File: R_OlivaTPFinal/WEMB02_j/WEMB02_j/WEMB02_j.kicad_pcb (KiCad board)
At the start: 2 copper layers, 164 x 139 mm, 97 parts, among them J201 Conn_01x05, J202 RasPI_IO_Header, J203 RS485, J301 EXP_PWR, Q201 IRFR9024, Q301 BC817-40_215, Q302 BC817-40_215, Q401 MMBTA42LT1G, U201 SN75HVD08, U301 SDM30-125S, U302 FEEDER_BRD, U303 R-78E3.3-0.5, U304 R-78E5.0-1.0, U401 ICL7665ACSA+

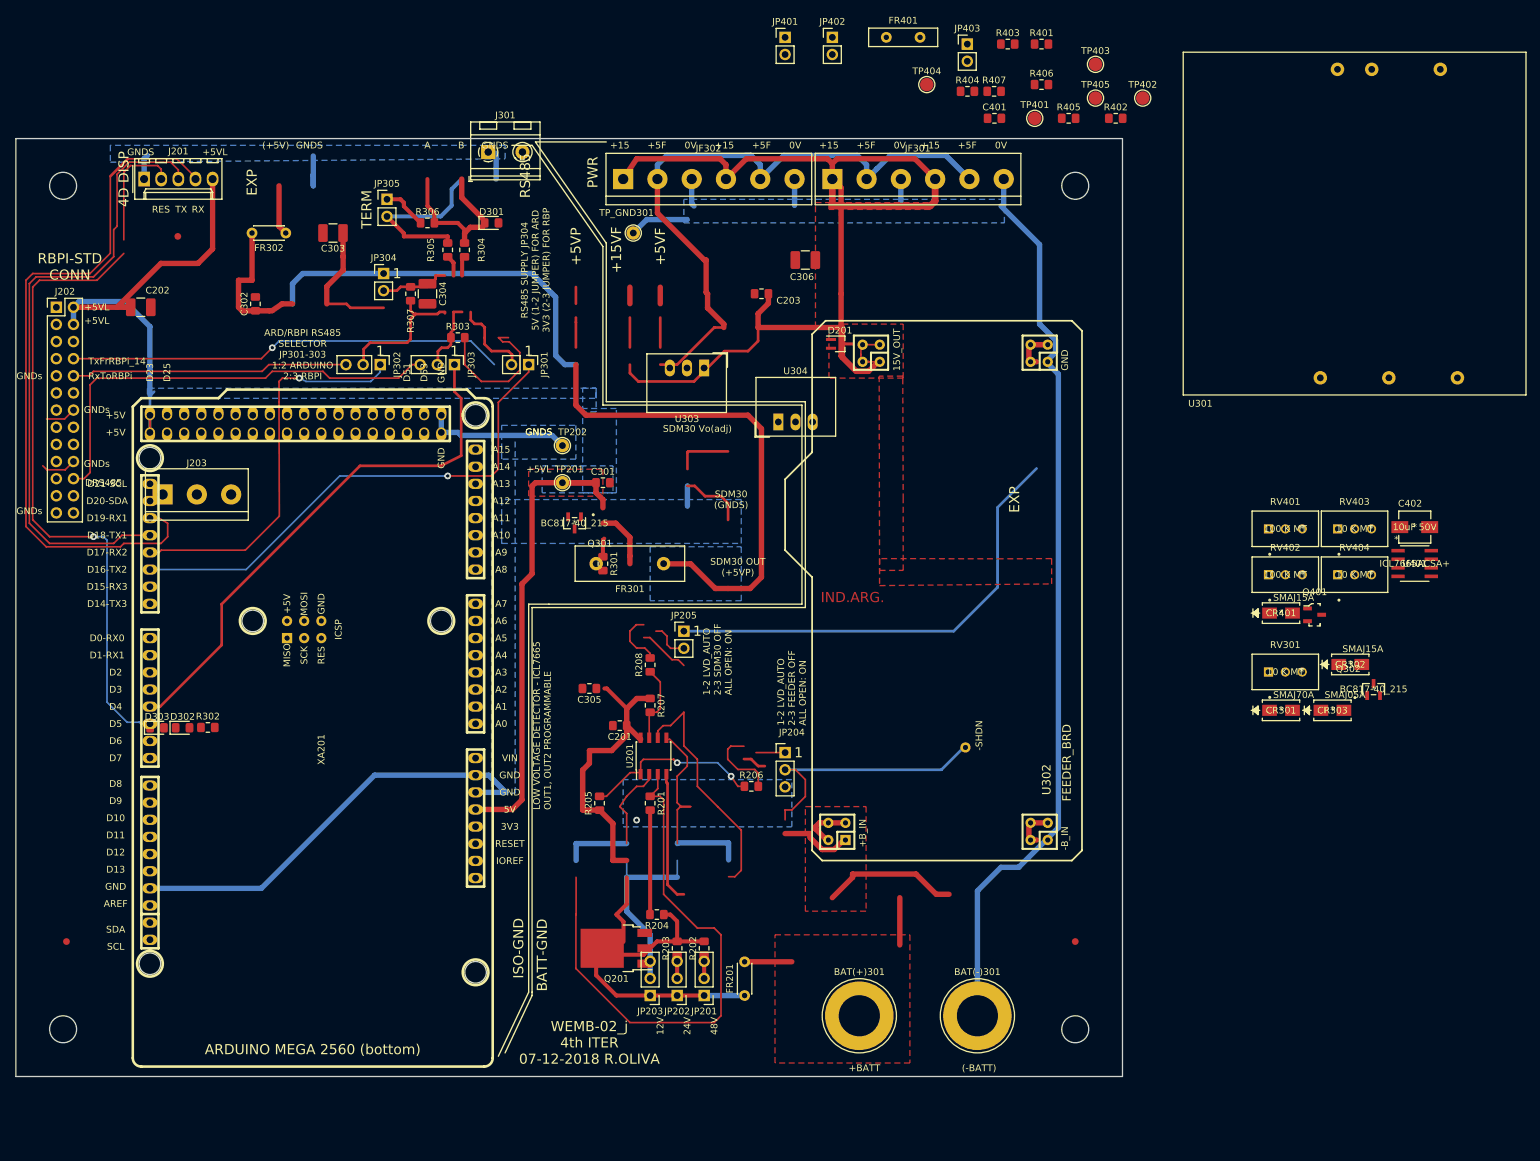
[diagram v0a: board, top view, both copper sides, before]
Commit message: WEMB02-J Sch + PCB completos, faltan algunos mod.3D
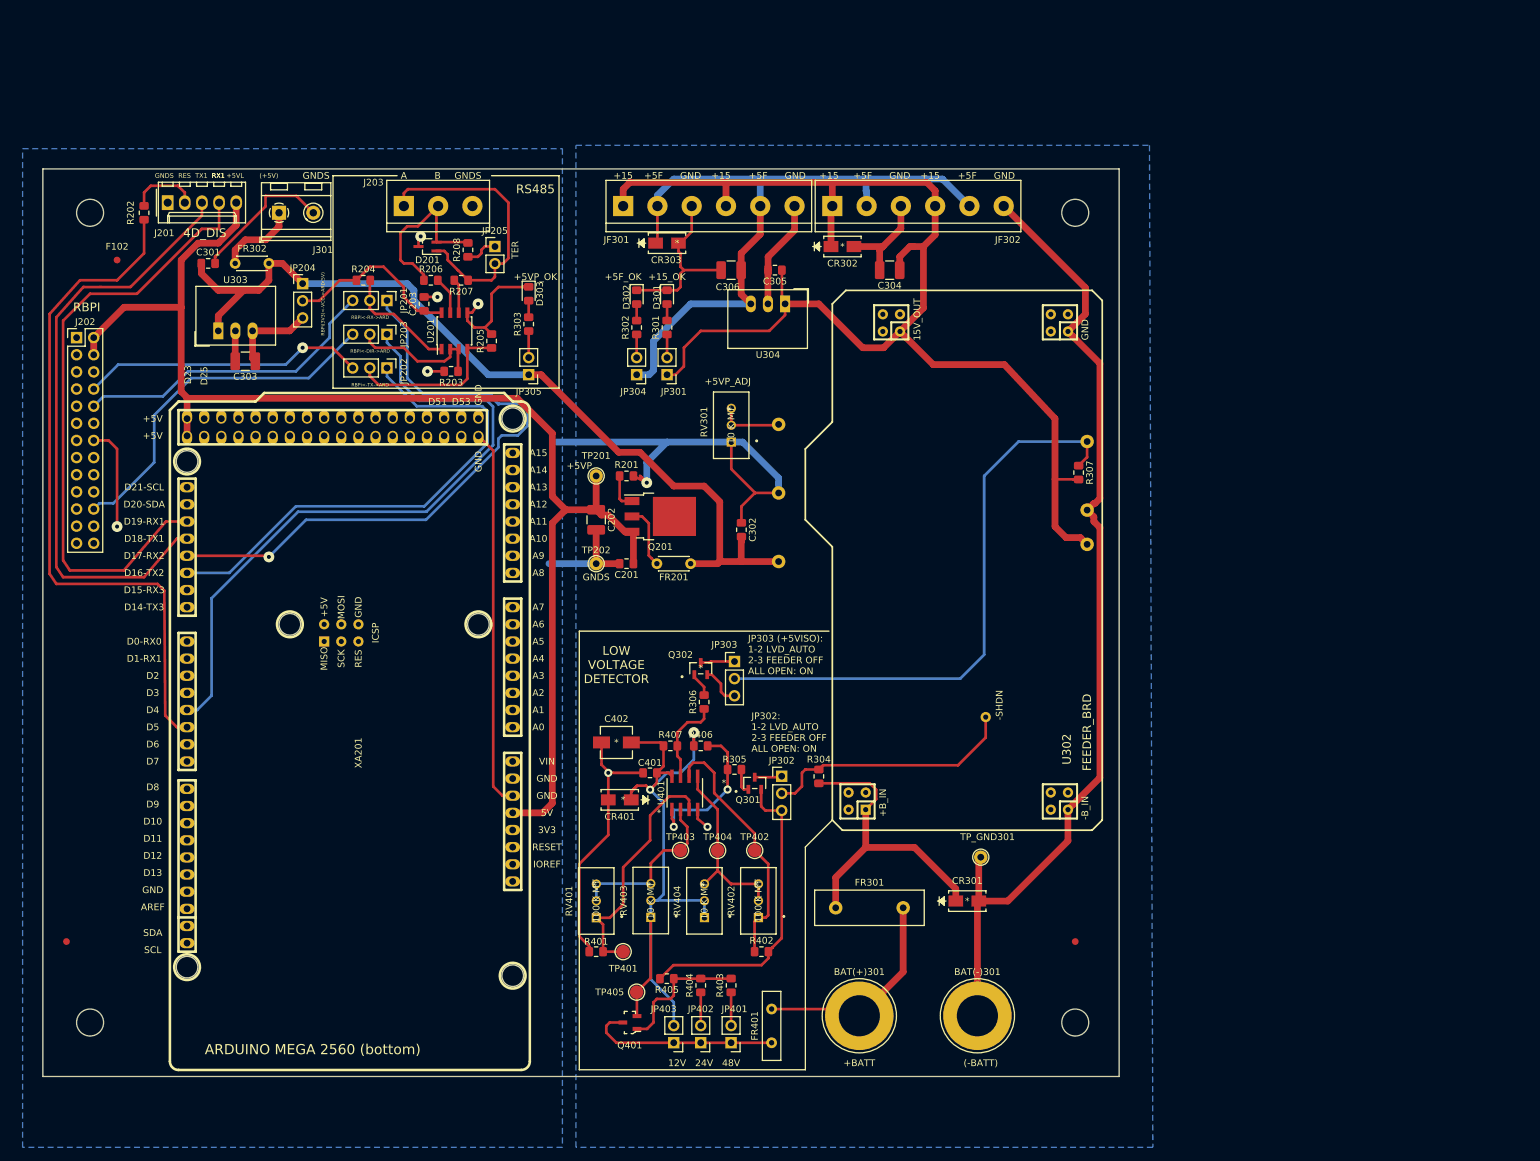
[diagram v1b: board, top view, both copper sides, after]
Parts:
- U301: moved to B.Cu
- moved JP403 154.3 mm to (158.5, 155.0), turned to 180 degrees
- moved JP402 150.3 mm to (162.5, 155.0), turned to 180 degrees
- moved FR401 150.0 mm to (173.0, 155.0), turned to 90 degrees
- moved R401 149.8 mm to (147.0, 141.5), turned to 180 degrees
- moved JP401 149.2 mm to (167.0, 155.0), turned to 180 degrees
- moved TP405 148.9 mm to (153.0, 147.5)
- moved R403 145.4 mm to (167.0, 146.5), turned to 90 degrees
- moved R405 140.7 mm to (157.5, 145.5), turned to 180 degrees
- moved R404 138.3 mm to (162.5, 146.5), turned to 90 degrees
- moved TP401 137.7 mm to (151.0, 141.5)
- moved R202 137.0 mm to (80.0, 32.0), turned to 270 degrees
- moved R402 134.2 mm to (171.5, 141.5)
- moved TP403 131.7 mm to (159.5, 126.5)
- moved TP402 125.5 mm to (170.5, 126.5)
- moved C402 122.5 mm to (150.0, 110.5), turned to 180 degrees
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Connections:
- JP403 pad 1: /LowV_Detect/+B_LVD -> Net-(FR401-Pad1)
- JP403 pad 2: Net-(FR401-Pad1) -> /LowV_Detect/+B_LVD
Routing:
- net +5VP: track 25.8 -> 132.8 mm
- net Earth: track 191.6 -> 297.5 mm, vias 1 -> 2
- net Net-(R202-Pad2): track 0.00 -> 102.0 mm
- net /LowV_Detect/+B_LVD: track 0.00 -> 99.3 mm, vias 0 -> 2
- net Net-(R213-Pad2): track 94.0 -> 0.00 mm, vias 1 -> 0
- net /Power/SDM_ON: track 0.00 -> 86.4 mm
- net /Power/V+_Q_EMIT: track 83.6 -> 0.00 mm
- net /Power/SET1_IN: track 81.9 -> 0.00 mm
- net Net-(JP205-Pad1): track 69.2 -> 4.92 mm
- net GNDS: track 143.5 -> 206.6 mm, vias 0 -> 6
- net /Power/+B_FEED: track 107.5 -> 46.6 mm
- net +5F: track 154.4 -> 104.3 mm
- net +5VL: track 150.3 -> 197.6 mm
- net /Power/-FSHDN: track 0.00 -> 37.9 mm
- net Net-(R402-Pad1): track 0.00 -> 37.3 mm
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- removed copper zone on F.Cu, net +15V
- removed copper zone on B.Cu, net +5VL
- removed copper zone on F.Cu, net +5VL
- removed copper zone on B.Cu, net +5VP
- removed copper zone on F.Cu, net /Power/+B_FEED
- removed copper zone on F.Cu, net /Power/BAT+
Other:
- board size 164 x 139 mm -> 159.5 x 134.5 mm
- rule trace_min: 0.2 -> 0.4
- rule via_min_drill: 0.3 -> 0.6
- rule via_min_size: 0.4 -> 1.2
- board text added: "+15_OK"
- board text added: "+5F_OK"
- board text added: "+5VP_ADJ"
- board text added: "+5VP_OK"
- board text added: "4D_DIS"
- board text added: "GND"
- board text added: "Grilla 1 mmPos / 0.5 mm ruteo. Pista 0.4mm. Margen: 0,4 mm. Vías: 1,2 / 0,6mm Fabricación en Mayer S.A. FR4 doble lado 1oz"
- board text added: "JP302: 1-2 LVD_AUTO 2-3 FEEDER OFF ALL OPEN: ON"
- board text added: "JP303 (+5VISO): 1-2 LVD_AUTO 2-3 FEEDER OFF ALL OPEN: ON"
- board text added: "LOW VOLTAGE DETECTOR"
- board text added: "RBPI"
- board text added: "RBPi(3V3)<-VCC->ARD(5V)"
- board text added: "RBPi<-DIR->ARD"
- board text added: "RBPi<-RX->ARD"
- board text added: "RBPi<-TX->ARD"
- board text added: "RX1"
- board text added: "TER"
- board text added: "TX1"
- board text removed: "+15VF"
- board text removed: "+5VF"
- board text removed: "0V"
- board text removed: "1"
- board text removed: "1-2 LVD_AUTO 2-3 FEEDER OFF ALL OPEN: ON"
- board text removed: "1-2 LVD_AUTO 2-3 SDM30 OFF ALL OPEN: ON"
- board text removed: "4D DISP"
- board text removed: "ARD/RBPI RS485 SELECTOR JP301-303 1:2 ARDUINO 2:3 RBPI"
- board text removed: "BATT-GND"
- board text removed: "DRS485"
- board text removed: "EXP"
- board text removed: "GNDs"
- board text removed: "Grilla 1 mmPos / 0.5 mm ruteo. Pista 0.25mm. Margen: 0,25 mm. Vías: 1 / 0,5mm Fabricación en Mayer S.A. FR4 doble lado 1oz"
- board text removed: "IND.ARG."
- board text removed: "ISO-GND"
- board text removed: "LOW VOLTAGE DETECTOR - ICL7665 OUT1, OUT2 PROGRAMMABLE"
- board text removed: "PWR"
- board text removed: "RBPI-STD CONN"
- board text removed: "RS485 SUPPLY JP304 5V (1-2 JUMPER) FOR ARD 3V3 (2-3 JUMPER) FOR RBP"
- board text removed: "RX"
- board text removed: "RxToRBPi"
- board text removed: "SDM30 (GNDS)"
- board text removed: "SDM30 OUT (+5VP)"
- board text removed: "SDM30 Vo(adj)"
- board text removed: "TERM"
- board text removed: "TX"
- board text removed: "TxFrRBPi_14"
- board text removed: "WEMB-02_j 4th ITER 07-12-2018 R.OLIVA"

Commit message: Ultimas Modificaciones WEMB02-j 14.12.2018 3D & Logos added
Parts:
- added REF**: OSHW-Logo2_7.3x6mm_SilkScreen, Symbol:OSHW-Logo2_7.3x6mm_SilkScreen, F.Cu at (111.5, 136.0)
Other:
- board text added: "12.2018"
- board text added: "IND.ARG. 2018"
- board text added: "PCB V02-J"
- board text added: "UNPA+L&R ING / R.OLIVA CESE 2018"
- board text added: "WIND EMPOWERMENT WEMB02"
